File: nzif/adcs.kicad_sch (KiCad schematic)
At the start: 18 parts, among them U1 ADAU1979xBCP, U201 ADA4807-1

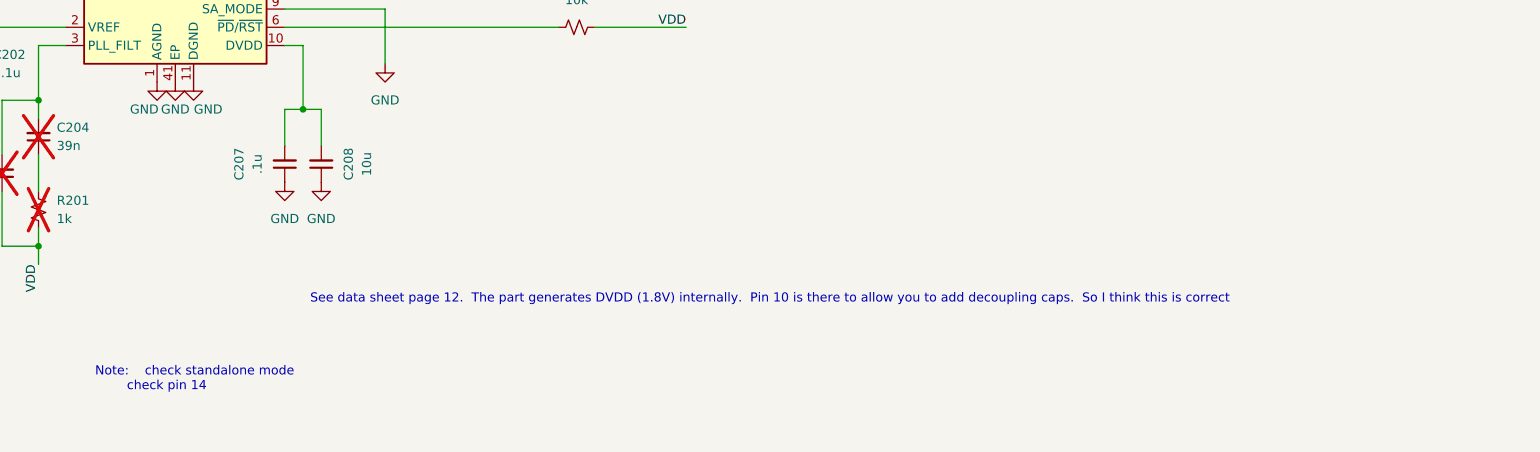
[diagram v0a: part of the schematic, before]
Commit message: Continue wiring DAC (Ref #29)
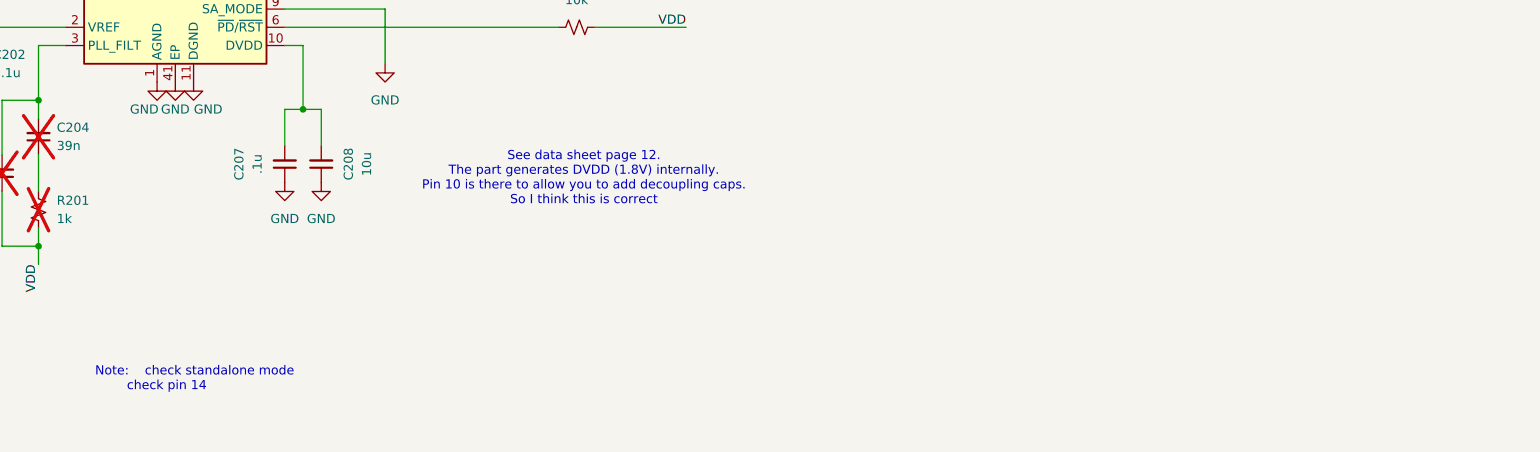
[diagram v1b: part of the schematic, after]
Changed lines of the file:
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@@
 		)
 	)
-	(text "See data sheet page 12.  The part generates DVDD (1.8V) internally.  Pin 10 is there to allow you to add decoupling caps.  So I think this is correct"
+	(text "See data sheet page 12.  \nThe part generates DVDD (1.8V) internally.  \nPin 10 is there to allow you to add decoupling caps.  \nSo I think this is correct"
 		(exclude_from_sim no)
-		(at 200.914 131.826 0)
+		(at 175.006 115.062 0)
 		(effects
 			(font

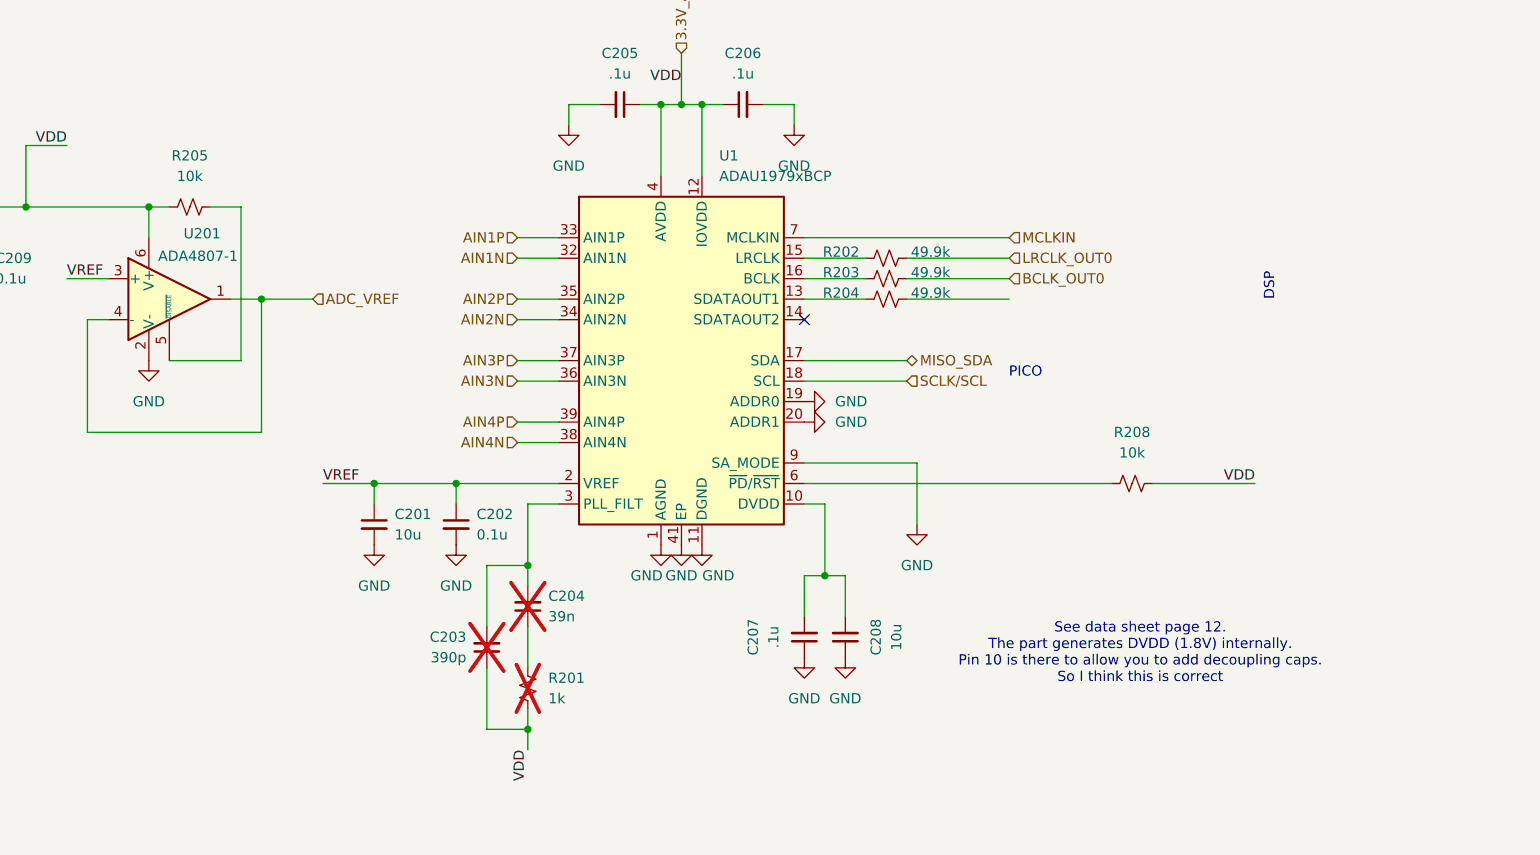
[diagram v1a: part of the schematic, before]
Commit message: updated dvdd and tdm bus
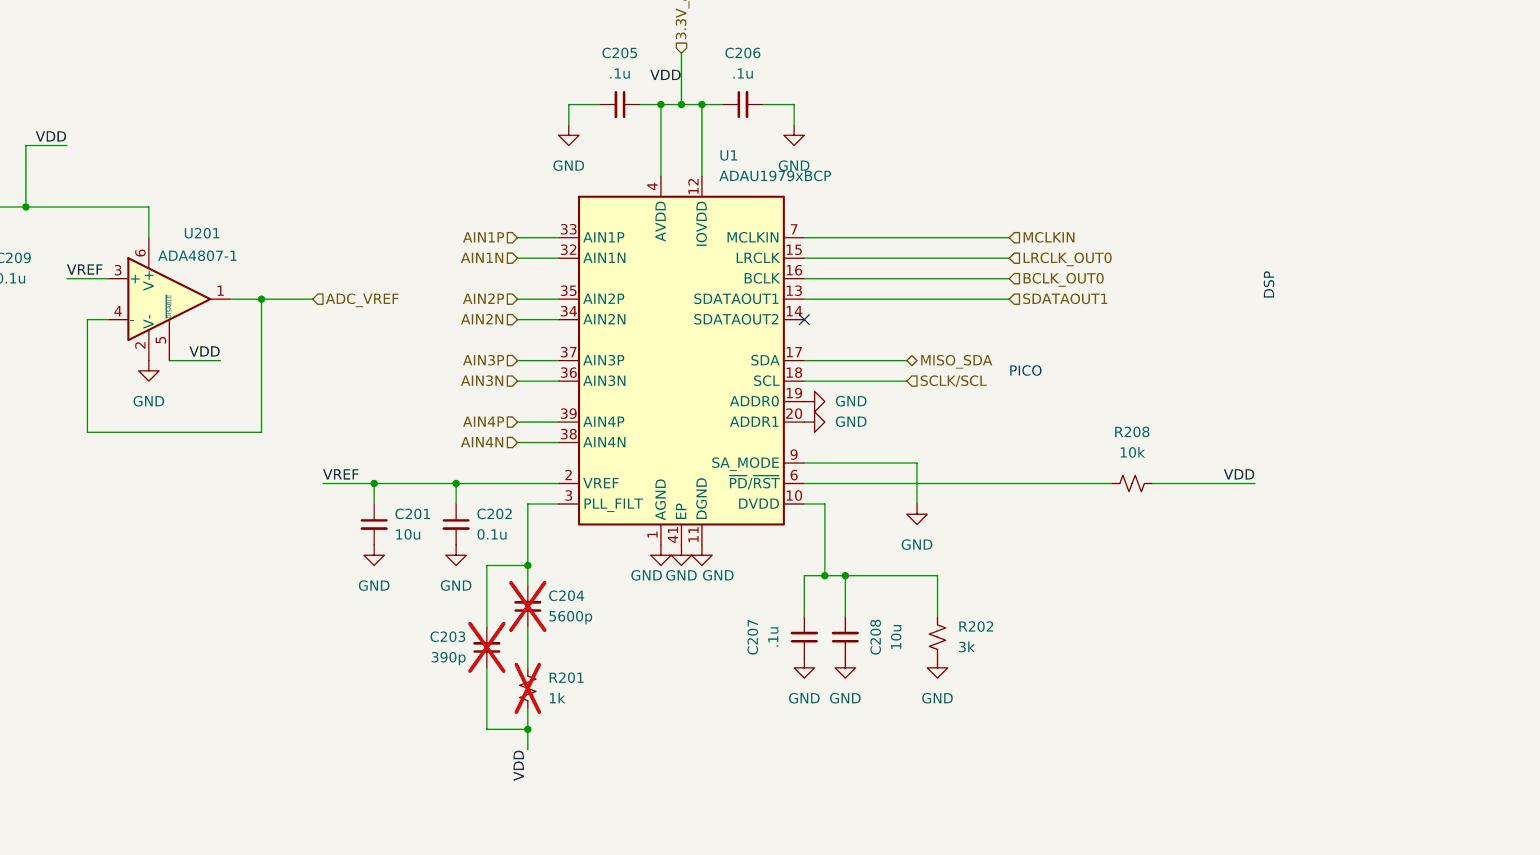
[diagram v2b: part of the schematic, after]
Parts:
- removed R203, R204: 49.9k, symbol Device:R_Small_US
- removed R205: 10k, Resistor_SMD:R_0603_1608Metric, symbol Device:R_Small_US
- C204: value 39n -> 5600p
- R202: value 49.9k -> 3k
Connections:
- net 3.3V_ADCs: now also U201.5 (~{DISABLE})
- net BCLK_OUT0: now also U1.16 (BCLK)
- net GND: now also R202.1
- net LRCLK_OUT0: now also U1.15 (LRCLK); no longer R202.2
- net at C207.2, C208.2, U1.10 (DVDD): now also R202.2
- net SDATAOUT1: now reaches U1.13 (SDATAOUT1)
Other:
- note removed: "See data sheet page 12. The part generates DVDD (1.8V) internally. Pin 10 is there to allow you to add decoupling caps. So I think this is correct"

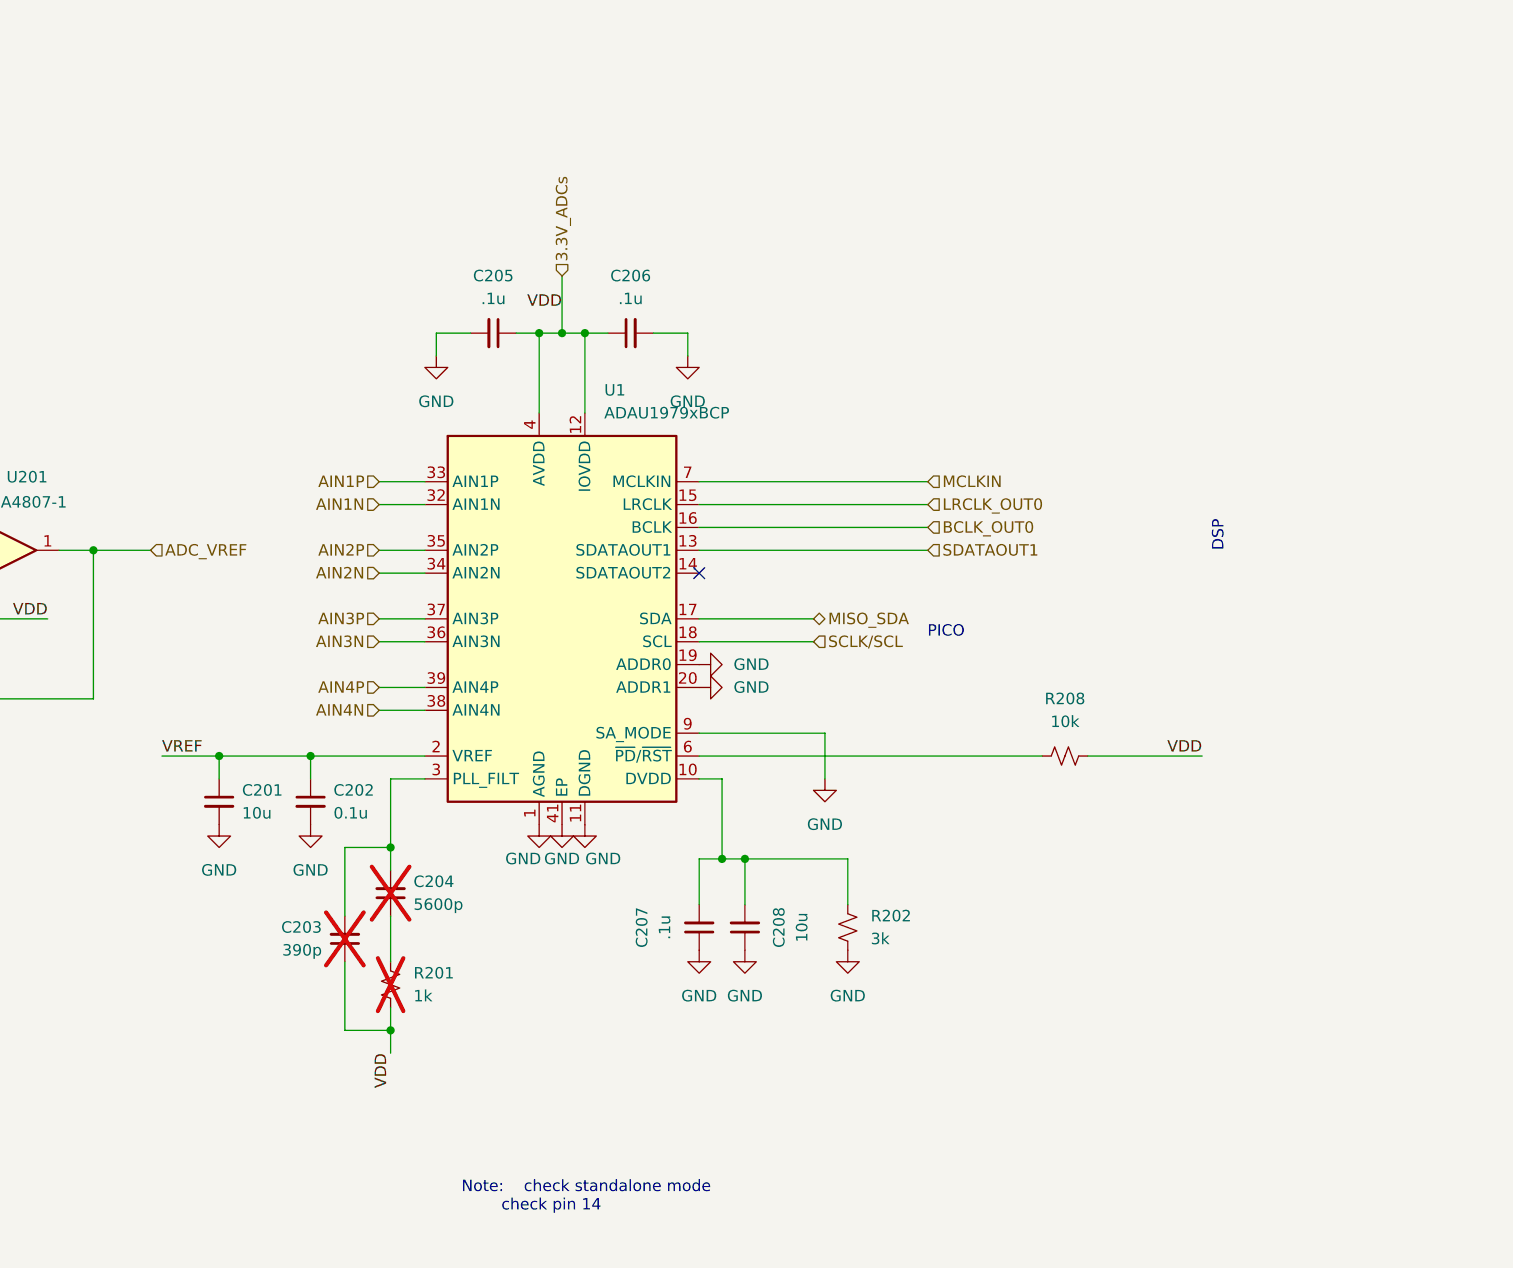
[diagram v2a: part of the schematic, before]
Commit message: updates to adau 1979 (Ref#33)
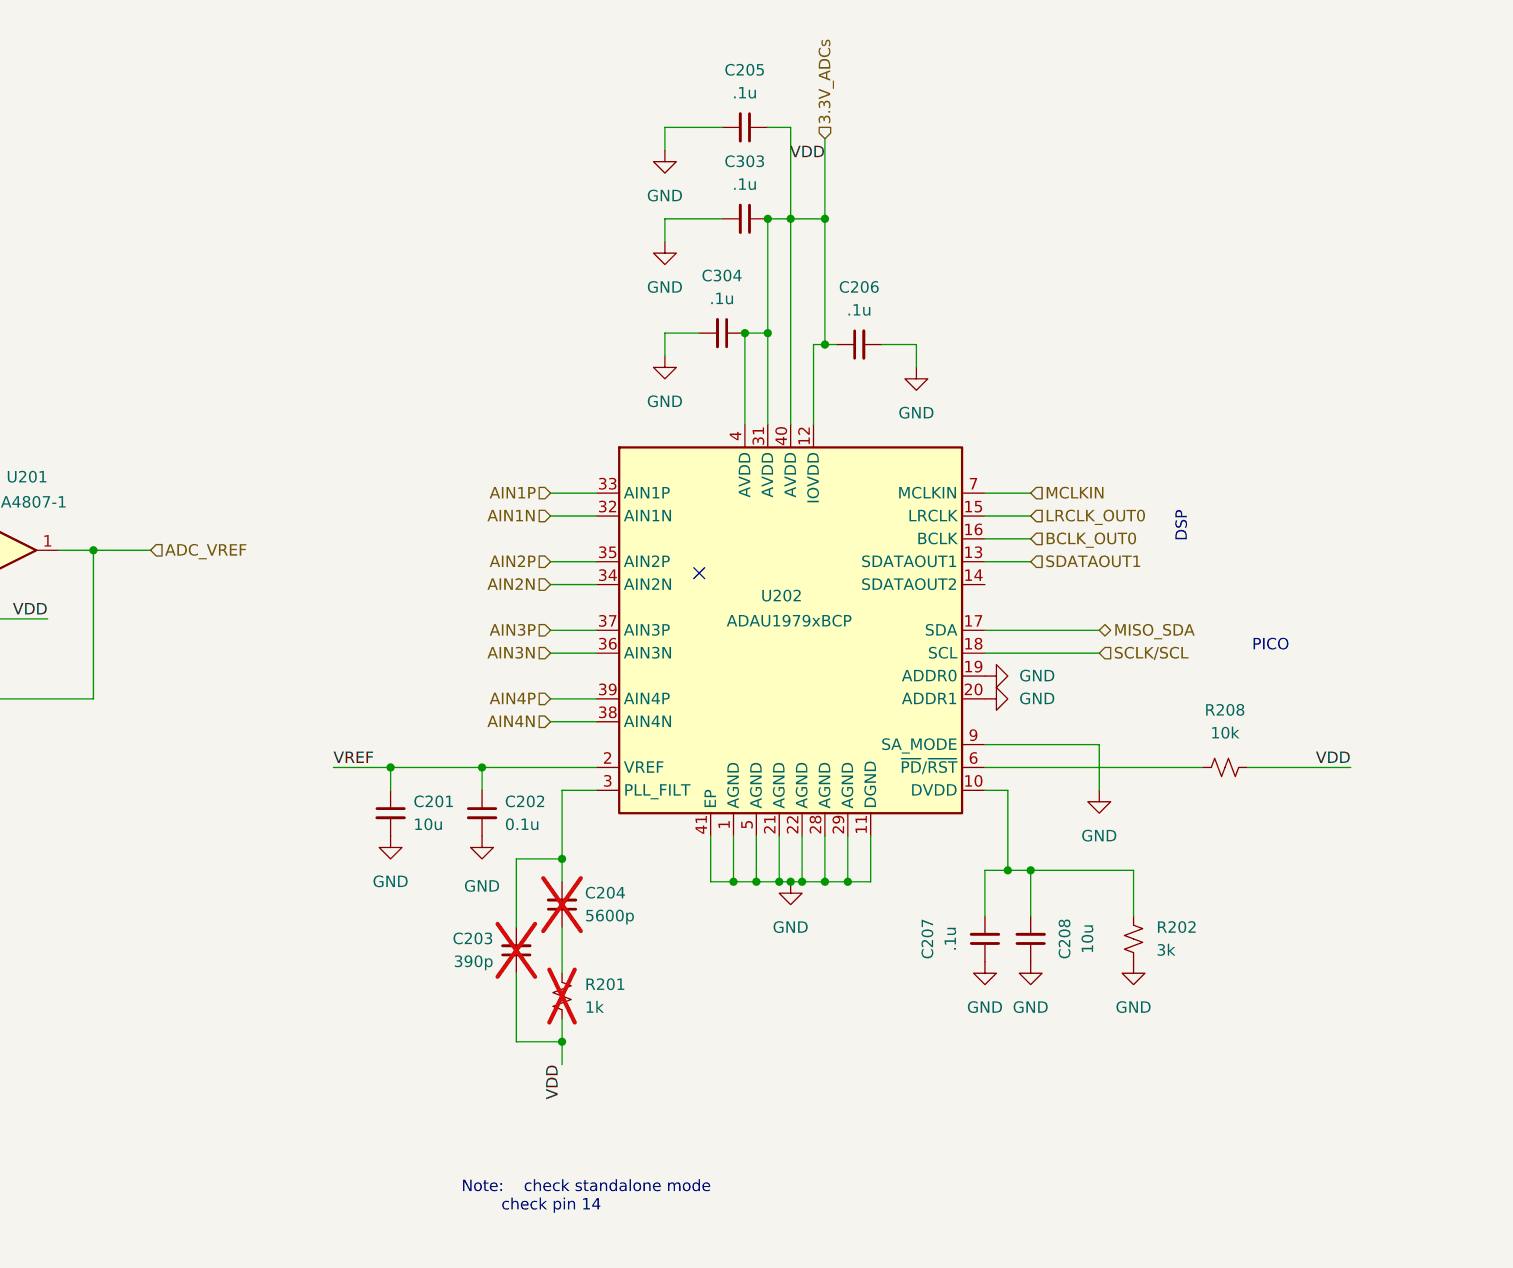
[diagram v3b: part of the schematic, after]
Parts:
- removed U1: ADAU1979xBCP, Package_CSP:LFCSP-40-1EP_6x6mm_P0.5mm_EP3.9x3.9mm, symbol Audio:ADAU1979xBCP
- added C303, C304: .1u, symbol Device:C_Small
- added U202: ADAU1979xBCP, Package_CSP:LFCSP-40-1EP_6x6mm_P0.5mm_EP3.9x3.9mm, symbol nzif_radio_symbol_library:ADAU1979xBCP
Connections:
- net 3.3V_ADCs: now also C303.1, C304.1, U202.12 (IOVDD), U202.31 (AVDD), U202.4 (AVDD), U202.40 (AVDD)
- net AIN1N: now also U202.32 (AIN1N)
- net AIN1P: now also U202.33 (AIN1P)
- net AIN2N: now also U202.34 (AIN2N)
- net AIN2P: now also U202.35 (AIN2P)
- net AIN3N: now also U202.36 (AIN3N)
- net AIN3P: now also U202.37 (AIN3P)
- net AIN4N: now also U202.38 (AIN4N)
- net AIN4P: now also U202.39 (AIN4P)
- net BCLK_OUT0: now also U202.16 (BCLK)
- net GND: now also C303.2, C304.2, U202.1 (AGND), U202.11 (DGND), U202.19 (ADDR0), U202.20 (ADDR1), U202.21 (AGND), U202.22 (AGND), U202.28 (AGND), U202.29 (AGND), U202.41 (EP), U202.5 (AGND), U202.9 (SA_MODE)
- net LRCLK_OUT0: now also U202.15 (LRCLK)
- net MCLKIN: now also U202.7 (MCLKIN)
- net MISO_SDA: now also U202.17 (SDA)
- net SCLK/SCL: now also U202.18 (SCL)
- net SDATAOUT1: now also U202.13 (SDATAOUT1)
- net VREF: now also U202.2 (VREF)
- net at C203.2, C204.2: now also U202.3 (PLL_FILT)
- net at C207.2, C208.2, R202.2: now also U202.10 (DVDD)
- net at R208.1: now also U202.6 (~{PD}/~{RST})
- new net: U202.23 (NC), U202.24 (NC), U202.25 (NC), U202.26 (NC), U202.27 (NC), U202.30 (NC), U202.8 (NC)
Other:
- moved on the sheet: C201, C202, C203, C204, C205, C206, C207, C208, R201, R202, R208

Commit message: completed adc review
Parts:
- removed C206, C303, C304: .1u, symbol Device:C_Small
- added C1, C2, C3: .1u, symbol Device:C_Small
- added C4: 10u, symbol Device:C_Small
- R?: renamed from R208; value 10k -> 47k
- renumbered C209 to C?, C204 to C?, C207 to C?, C201 to C?, C203 to C?, C210 to C?, C208 to C?, C205 to C?, C202 to C?, R201 to R?, R202 to R?, U201 to U?, U202 to U?
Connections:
- net 3.3V_ADCs: now also C1.1, C2.1, C3.1, C4.1
- net GND: now also C1.2, C2.2, C3.2, C4.2
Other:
- note removed: "Note: check standalone mode check pin 14"
- moved on the sheet: C?, R?, U?
